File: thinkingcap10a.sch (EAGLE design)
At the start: 14 parts, among them IC1 ATMEGA644M, IC2 AD811E, Q1 2N4416

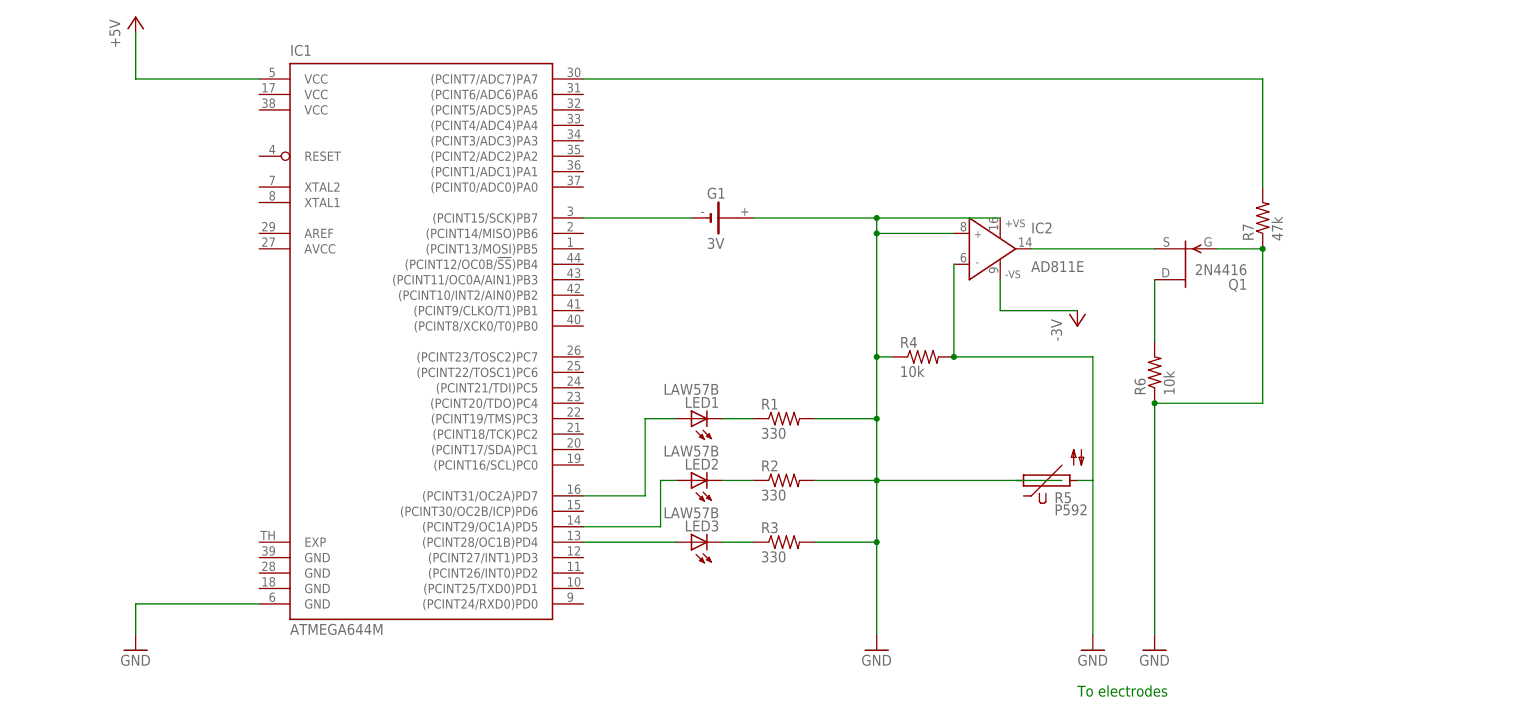
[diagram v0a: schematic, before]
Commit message: 
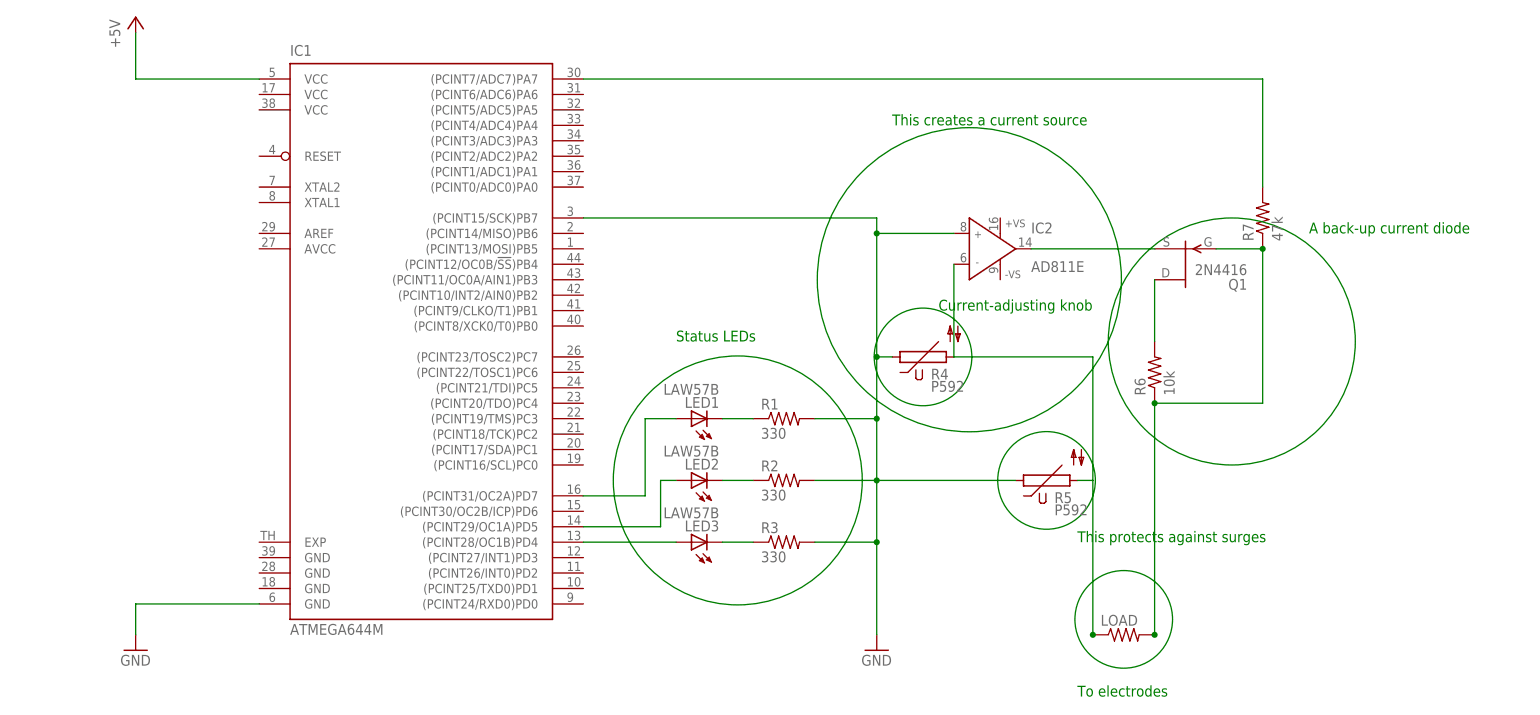
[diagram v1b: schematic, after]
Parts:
- removed G1: 3V, battery:1V60R
- added LOAD: (no value), rcl:R-US_0204/2V
- R4: value 10k -> P592; device rcl:R-US_0204/2V -> varistor:P592
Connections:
- removed net -5V: IC2.-VS
- removed net N$7: G1.-, IC1.(PCINT15/SCK)PB7
- new net N$12: LOAD.2, Q1.G, R6.1, R7.1
- new net N$8: IC2.IN-, LOAD.1
- net GND: now also IC1.(PCINT15/SCK)PB7; no longer G1.+, IC2.+VS, IC2.IN-, Q1.G, R4.1, R4.2, R6.1, R7.1
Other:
- note added: "A back-up current diode"
- note added: "Current-adjusting knob"
- note added: "Status LEDs"
- note added: "This creates a current source"
- note added: "This protects against surges"
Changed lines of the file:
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@@
 <part name="R2" library="rcl" deviceset="R-US_" device="0204/2V" value="330"/>
 <part name="R3" library="rcl" deviceset="R-US_" device="0204/2V" value="330"/>
-<part name="G1" library="battery" deviceset="1V60R" device="" value="3V"/>
 <part name="IC2" library="analog-devices" deviceset="AD811" device="E"/>
-<part name="GND3" library="supply1" deviceset="GND" device=""/>
-<part name="GND4" library="supply1" deviceset="GND" device=""/>
-<part name="R4" library="rcl" deviceset="R-US_" device="0204/2V" value="10k"/>
-<part name="P-1" library="supply1" deviceset="-5V" device="" value="-3V"/>
 <part name="R5" library="varistor" deviceset="P592" device=""/>
 <part name="Q1" library="transistor-fet" deviceset="2N4416" device=""/>
 <part name="R6" library="rcl" deviceset="R-US_" device="0204/2V" value="10k"/>
 <part name="R7" library="rcl" deviceset="R-US_" device="0204/2V" value="47k"/>
+<part name="LOAD" library="rcl" deviceset="R-US_" device="0204/2V"/>
+<part name="R4" library="varistor" deviceset="P592" device=""/>
 </parts>
 <sheets>
@@
 <plain>
 <text x="182.88" y="-17.78" size="1.778" layer="91">To electrodes</text>
+<circle x="127" y="17.78" radius="20.478134375" width="0.1524" layer="91"/>
+<text x="116.84" y="40.64" size="1.778" layer="91">Status LEDs</text>
+<circle x="165.1" y="50.8" radius="25.016096875" width="0.1524" layer="91"/>
+<text x="152.4" y="76.2" size="1.778" layer="91">This creates a current source</text>
+<circle x="157.48" y="38.1" radius="8.032184375" width="0.1524" layer="91"/>
+<text x="160.02" y="45.72" size="1.778" layer="91">Current-adjusting knob</text>
+<circle x="190.5" y="-5.08" radius="8.032184375" width="0.1524" layer="91"/>
+<circle x="177.8" y="17.78" radius="8.032184375" width="0.1524" layer="91"/>
+<text x="182.88" y="7.62" size="1.778" layer="91">This protects against surges</text>
+<circle x="208.28" y="40.64" radius="20.32" width="0.1524" layer="91"/>
+<text x="220.98" y="58.42" size="1.778" layer="91">A back-up current diode</text>
 </plain>
 <instances>
@@
 <instance part="R2" gate="G$1" x="134.62" y="17.78"/>
 <instance part="R3" gate="G$1" x="134.62" y="7.62"/>
-<instance part="G1" gate="1" x="124.46" y="60.96"/>
 <instance part="IC2" gate="G$" x="167.64" y="55.88"/>
-<instance part="GND3" gate="1" x="195.58" y="-10.16"/>
-<instance part="GND4" gate="1" x="185.42" y="-10.16"/>
-<instance part="R4" gate="G$1" x="157.48" y="38.1"/>
-<instance part="P-1" gate="1" x="182.88" y="43.18"/>
 <instance part="R5" gate="1" x="177.819465625" y="17.7656625"/>
 <instance part="Q1" gate="G$1" x="200.66" y="53.34" rot="R180"/>
 <instance part="R6" gate="G$1" x="195.58" y="35.56" rot="R90"/>
 <instance part="R7" gate="G$1" x="213.36" y="60.96" rot="R90"/>
+<instance part="LOAD" gate="G$1" x="190.5" y="-7.62"/>
+<instance part="R4" gate="1" x="157.499465625" y="38.0856625"/>
 </instances>
 <busses>
@@
 <junction x="149.86" y="38.1"/>
 <wire x1="149.86" y1="38.1" x2="149.86" y2="27.94" width="0.1524" layer="91"/>
-<pinref part="R4" gate="G$1" pin="1"/>
 <wire x1="152.4" y1="38.1" x2="149.86" y2="38.1" width="0.1524" layer="91"/>
-<wire x1="180.34" y1="17.78" x2="149.86" y2="17.78" width="0.1524" layer="91"/>
-<pinref part="G1" gate="1" pin="+"/>
-<pinref part="IC2" gate="G$" pin="+VS"/>
-<wire x1="129.54" y1="60.96" x2="149.86" y2="60.96" width="0.1524" layer="91"/>
-<wire x1="149.86" y1="60.96" x2="170.18" y2="60.96" width="0.1524" layer="91"/>
 <wire x1="149.86" y1="60.96" x2="149.86" y2="58.42" width="0.1524" layer="91"/>
 <junction x="149.86" y="58.42"/>
-<junction x="149.86" y="60.96"/>
-</segment>
-<segment>
-<pinref part="GND4" gate="1" pin="GND"/>
-<wire x1="185.42" y1="-7.62" x2="185.42" y2="17.78" width="0.1524" layer="91"/>
-<wire x1="185.42" y1="17.78" x2="185.42" y2="38.1" width="0.1524" layer="91"/>
-<wire x1="185.42" y1="38.1" x2="162.56" y2="38.1" width="0.1524" layer="91"/>
-<pinref part="IC2" gate="G$" pin="IN-"/>
-<wire x1="162.56" y1="38.1" x2="162.56" y2="53.34" width="0.1524" layer="91"/>
-<junction x="162.56" y="38.1"/>
-<pinref part="R4" gate="G$1" pin="2"/>
-<wire x1="182.88" y1="17.78" x2="185.42" y2="17.78" width="0.1524" layer="91"/>
-</segment>
-<segment>
-<pinref part="Q1" gate="G$1" pin="G"/>
-<pinref part="GND3" gate="1" pin="GND"/>
-<pinref part="R6" gate="G$1" pin="1"/>
-<junction x="195.58" y="30.48"/>
-<wire x1="195.58" y1="30.48" x2="195.58" y2="-7.62" width="0.1524" layer="91"/>
-<wire x1="195.58" y1="30.48" x2="213.36" y2="30.48" width="0.1524" layer="91"/>
-<wire x1="213.36" y1="30.48" x2="213.36" y2="55.88" width="0.1524" layer="91"/>
-<wire x1="213.36" y1="55.88" x2="205.74" y2="55.88" width="0.1524" layer="91"/>
-<pinref part="R7" gate="G$1" pin="1"/>
-<junction x="213.36" y="55.88"/>
+<wire x1="149.86" y1="17.78" x2="172.72" y2="17.78" width="0.1524" layer="91"/>
+<pinref part="IC1" gate="G$1" pin="(PCINT15/SCK)PB7"/>
+<wire x1="101.6" y1="60.96" x2="149.86" y2="60.96" width="0.1524" layer="91"/>
 </segment>
 </net>
@@
 <pinref part="R3" gate="G$1" pin="1"/>
 <wire x1="124.46" y1="7.62" x2="129.54" y2="7.62" width="0.1524" layer="91"/>
-</segment>
-</net>
-<net name="N$7" class="0">
-<segment>
-<pinref part="IC1" gate="G$1" pin="(PCINT15/SCK)PB7"/>
-<wire x1="101.6" y1="60.96" x2="119.38" y2="60.96" width="0.1524" layer="91"/>
-<pinref part="G1" gate="1" pin="-"/>
 </segment>
 </net>
@@
 </segment>
 </net>
-<net name="-5V" class="0">
-<segment>
-<pinref part="IC2" gate="G$" pin="-VS"/>
-<wire x1="170.18" y1="50.8" x2="170.18" y2="45.72" width="0.1524" layer="91"/>
-<wire x1="170.18" y1="45.72" x2="182.88" y2="45.72" width="0.1524" layer="91"/>
-<pinref part="P-1" gate="1" pin="-5V"/>
-</segment>
-</net>
 <net name="N$9" class="0">
 <segment>
@@
 </segment>
 </net>
+<net name="N$8" class="0">
+<segment>
+<wire x1="185.42" y1="-7.62" x2="185.42" y2="17.78" width="0.1524" layer="91"/>
+<wire x1="185.42" y1="17.78" x2="185.42" y2="38.1" width="0.1524" layer="91"/>
+<wire x1="185.42" y1="38.1" x2="162.56" y2="38.1" width="0.1524" layer="91"/>
+<pinref part="IC2" gate="G$" pin="IN-"/>
+<wire x1="162.56" y1="38.1" x2="162.56" y2="53.34" width="0.1524" layer="91"/>
+<wire x1="182.88" y1="17.78" x2="185.42" y2="17.78" width="0.1524" layer="91"/>
+<junction x="185.42" y="-7.62"/>
+<pinref part="LOAD" gate="G$1" pin="1"/>
+</segment>
+</net>
+<net name="N$12" class="0">
+<segment>
+<pinref part="Q1" gate="G$1" pin="G"/>
+<pinref part="R6" gate="G$1" pin="1"/>
+<junction x="195.58" y="30.48"/>
+<wire x1="195.58" y1="30.48" x2="195.58" y2="-7.62" width="0.1524" layer="91"/>
+<wire x1="195.58" y1="30.48" x2="213.36" y2="30.48" width="0.1524" layer="91"/>
+<wire x1="213.36" y1="30.48" x2="213.36" y2="55.88" width="0.1524" layer="91"/>
+<wire x1="213.36" y1="55.88" x2="205.74" y2="55.88" width="0.1524" layer="91"/>
+<pinref part="R7" gate="G$1" pin="1"/>
+<junction x="213.36" y="55.88"/>
+<junction x="195.58" y="-7.62"/>
+<pinref part="LOAD" gate="G$1" pin="2"/>
+</segment>
+</net>

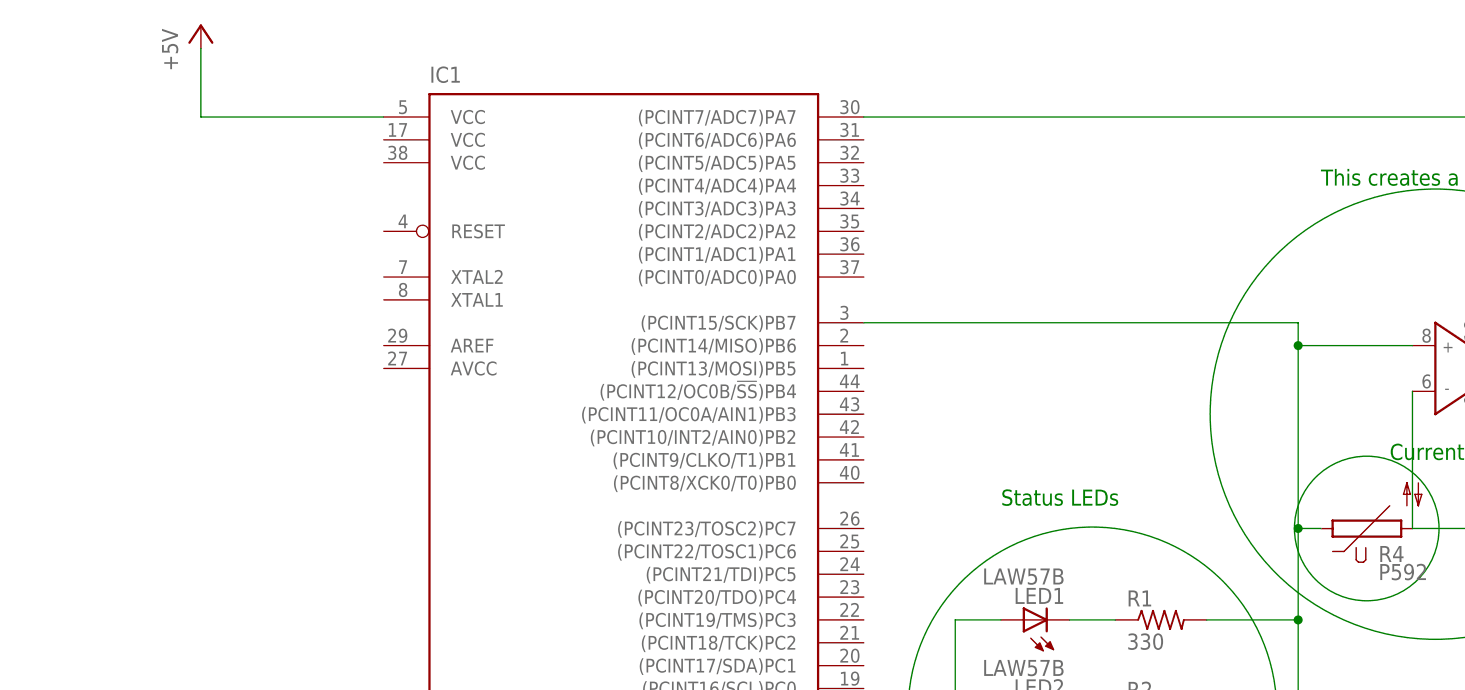
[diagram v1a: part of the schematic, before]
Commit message: Updated SCH (a) to v1.0
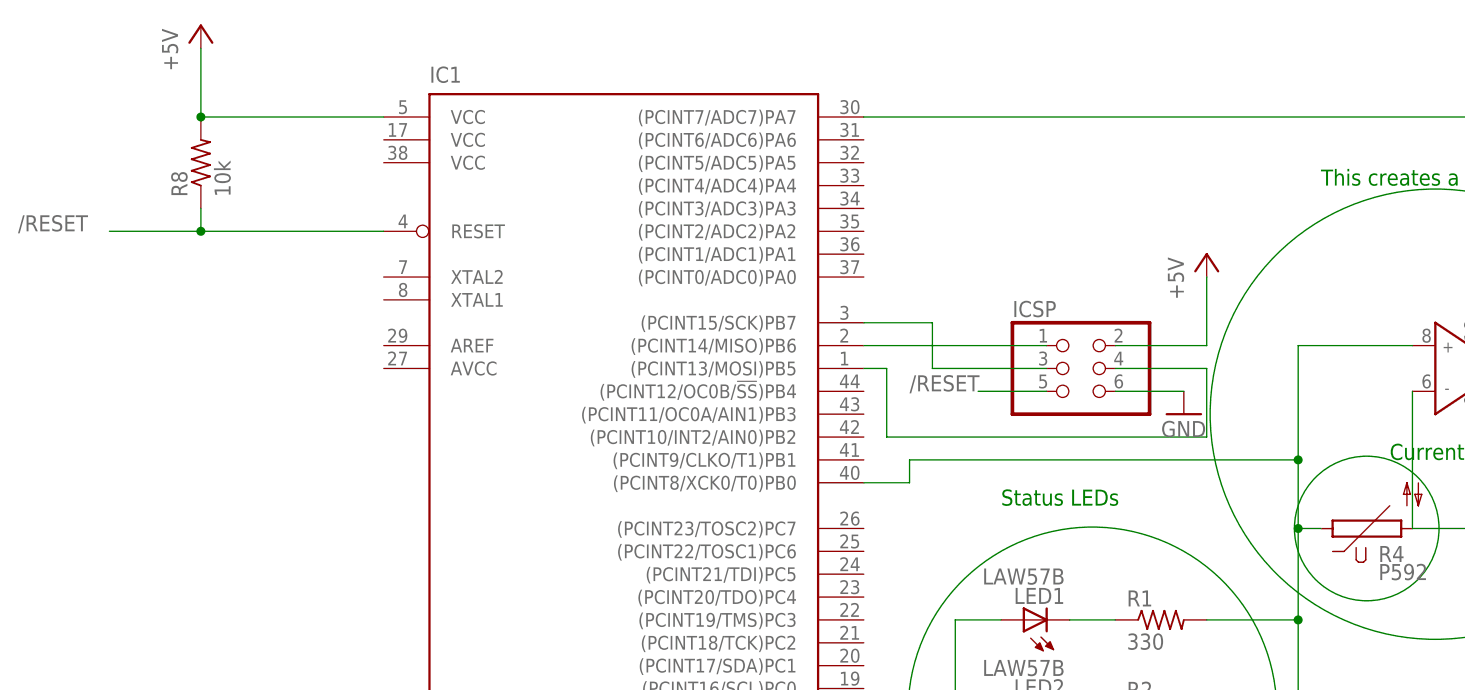
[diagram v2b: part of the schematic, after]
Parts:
- added ICSP: (no value), pinhead:PINHD-2X3/90
- added R8: 10k, rcl:R-US_0204/2V
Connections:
- new net /RESET: IC1.RESET, ICSP.5, R8.1
- new net N$13: IC1.(PCINT15/SCK)PB7, ICSP.3
- new net N$14: IC1.(PCINT13/MOSI)PB5, ICSP.4
- new net N$7: IC1.(PCINT14/MISO)PB6, ICSP.1
- net +5V: now also ICSP.2, R8.2
- net GND: now also IC1.(PCINT8/XCK0/T0)PB0, ICSP.6; no longer IC1.(PCINT15/SCK)PB7
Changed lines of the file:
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@@
 <part name="LOAD" library="rcl" deviceset="R-US_" device="0204/2V"/>
 <part name="R4" library="varistor" deviceset="P592" device=""/>
+<part name="ICSP" library="pinhead" deviceset="PINHD-2X3" device="/90"/>
+<part name="P+2" library="supply1" deviceset="+5V" device=""/>
+<part name="GND3" library="supply1" deviceset="GND" device=""/>
+<part name="R8" library="rcl" deviceset="R-US_" device="0204/2V" value="10k"/>
 </parts>
 <sheets>
@@
 <instance part="LOAD" gate="G$1" x="190.5" y="-7.62"/>
 <instance part="R4" gate="1" x="157.499465625" y="38.0856625"/>
+<instance part="ICSP" gate="A" x="124.46" y="55.88"/>
+<instance part="P+2" gate="1" x="139.7" y="68.58"/>
+<instance part="GND3" gate="1" x="137.16" y="50.8"/>
+<instance part="R8" gate="G$1" x="27.94" y="78.74" rot="R90"/>
 </instances>
 <busses>
@@
 <wire x1="27.94" y1="83.82" x2="27.94" y2="91.44" width="0.1524" layer="91"/>
 <pinref part="P+1" gate="1" pin="+5V"/>
+<pinref part="R8" gate="G$1" pin="2"/>
+<junction x="27.94" y="83.82"/>
+</segment>
+<segment>
+<pinref part="ICSP" gate="A" pin="2"/>
+<wire x1="129.54" y1="58.42" x2="139.7" y2="58.42" width="0.1524" layer="91"/>
+<pinref part="P+2" gate="1" pin="+5V"/>
+<wire x1="139.7" y1="58.42" x2="139.7" y2="66.04" width="0.1524" layer="91"/>
 </segment>
 </net>
@@
 <pinref part="IC2" gate="G$" pin="IN+"/>
 <wire x1="162.56" y1="58.42" x2="149.86" y2="58.42" width="0.1524" layer="91"/>
-<wire x1="149.86" y1="58.42" x2="149.86" y2="38.1" width="0.1524" layer="91"/>
+<wire x1="149.86" y1="58.42" x2="149.86" y2="45.72" width="0.1524" layer="91"/>
 <junction x="149.86" y="38.1"/>
+<wire x1="149.86" y1="45.72" x2="149.86" y2="38.1" width="0.1524" layer="91"/>
 <wire x1="149.86" y1="38.1" x2="149.86" y2="27.94" width="0.1524" layer="91"/>
 <wire x1="152.4" y1="38.1" x2="149.86" y2="38.1" width="0.1524" layer="91"/>
-<wire x1="149.86" y1="60.96" x2="149.86" y2="58.42" width="0.1524" layer="91"/>
-<junction x="149.86" y="58.42"/>
 <wire x1="149.86" y1="17.78" x2="172.72" y2="17.78" width="0.1524" layer="91"/>
-<pinref part="IC1" gate="G$1" pin="(PCINT15/SCK)PB7"/>
-<wire x1="101.6" y1="60.96" x2="149.86" y2="60.96" width="0.1524" layer="91"/>
+<junction x="149.86" y="45.72"/>
+<wire x1="149.86" y1="45.72" x2="106.68" y2="45.72" width="0.1524" layer="91"/>
+<wire x1="106.68" y1="45.72" x2="106.68" y2="43.18" width="0.1524" layer="91"/>
+<pinref part="IC1" gate="G$1" pin="(PCINT8/XCK0/T0)PB0"/>
+<wire x1="106.68" y1="43.18" x2="101.6" y2="43.18" width="0.1524" layer="91"/>
+</segment>
+<segment>
+<pinref part="ICSP" gate="A" pin="6"/>
+<wire x1="129.54" y1="53.34" x2="137.16" y2="53.34" width="0.1524" layer="91"/>
+<pinref part="GND3" gate="1" pin="GND"/>
 </segment>
 </net>
@@
 </segment>
 </net>
+<net name="N$7" class="0">
+<segment>
+<pinref part="ICSP" gate="A" pin="1"/>
+<pinref part="IC1" gate="G$1" pin="(PCINT14/MISO)PB6"/>
+<wire x1="121.92" y1="58.42" x2="101.6" y2="58.42" width="0.1524" layer="91"/>
+</segment>
+</net>
+<net name="N$13" class="0">
+<segment>
+<pinref part="ICSP" gate="A" pin="3"/>
+<wire x1="121.92" y1="55.88" x2="109.22" y2="55.88" width="0.1524" layer="91"/>
+<wire x1="109.22" y1="55.88" x2="109.22" y2="60.96" width="0.1524" layer="91"/>
+<pinref part="IC1" gate="G$1" pin="(PCINT15/SCK)PB7"/>
+<wire x1="109.22" y1="60.96" x2="101.6" y2="60.96" width="0.1524" layer="91"/>
+</segment>
+</net>
+<net name="N$14" class="0">
+<segment>
+<pinref part="ICSP" gate="A" pin="4"/>
+<wire x1="129.54" y1="55.88" x2="139.7" y2="55.88" width="0.1524" layer="91"/>
+<wire x1="139.7" y1="55.88" x2="139.7" y2="48.26" width="0.1524" layer="91"/>
+<wire x1="139.7" y1="48.26" x2="104.14" y2="48.26" width="0.1524" layer="91"/>
+<wire x1="104.14" y1="48.26" x2="104.14" y2="55.88" width="0.1524" layer="91"/>
+<pinref part="IC1" gate="G$1" pin="(PCINT13/MOSI)PB5"/>
+<wire x1="104.14" y1="55.88" x2="101.6" y2="55.88" width="0.1524" layer="91"/>
+</segment>
+</net>
+<net name="/RESET" class="0">
+<segment>
+<pinref part="IC1" gate="G$1" pin="RESET"/>
+<wire x1="48.26" y1="71.12" x2="27.94" y2="71.12" width="0.1524" layer="91"/>
+<wire x1="27.94" y1="71.12" x2="27.94" y2="73.66" width="0.1524" layer="91"/>
+<pinref part="R8" gate="G$1" pin="1"/>
+<wire x1="27.94" y1="71.12" x2="17.78" y2="71.12" width="0.1524" layer="91"/>
+<junction x="27.94" y="71.12"/>
+<label x="7.62" y="71.12" size="1.778" layer="95"/>
+</segment>
+<segment>
+<pinref part="ICSP" gate="A" pin="5"/>
+<wire x1="121.92" y1="53.34" x2="114.3" y2="53.34" width="0.1524" layer="91"/>
+<label x="106.68" y="53.34" size="1.778" layer="95"/>
+</segment>
+</net>
